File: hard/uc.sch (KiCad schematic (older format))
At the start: 1 part

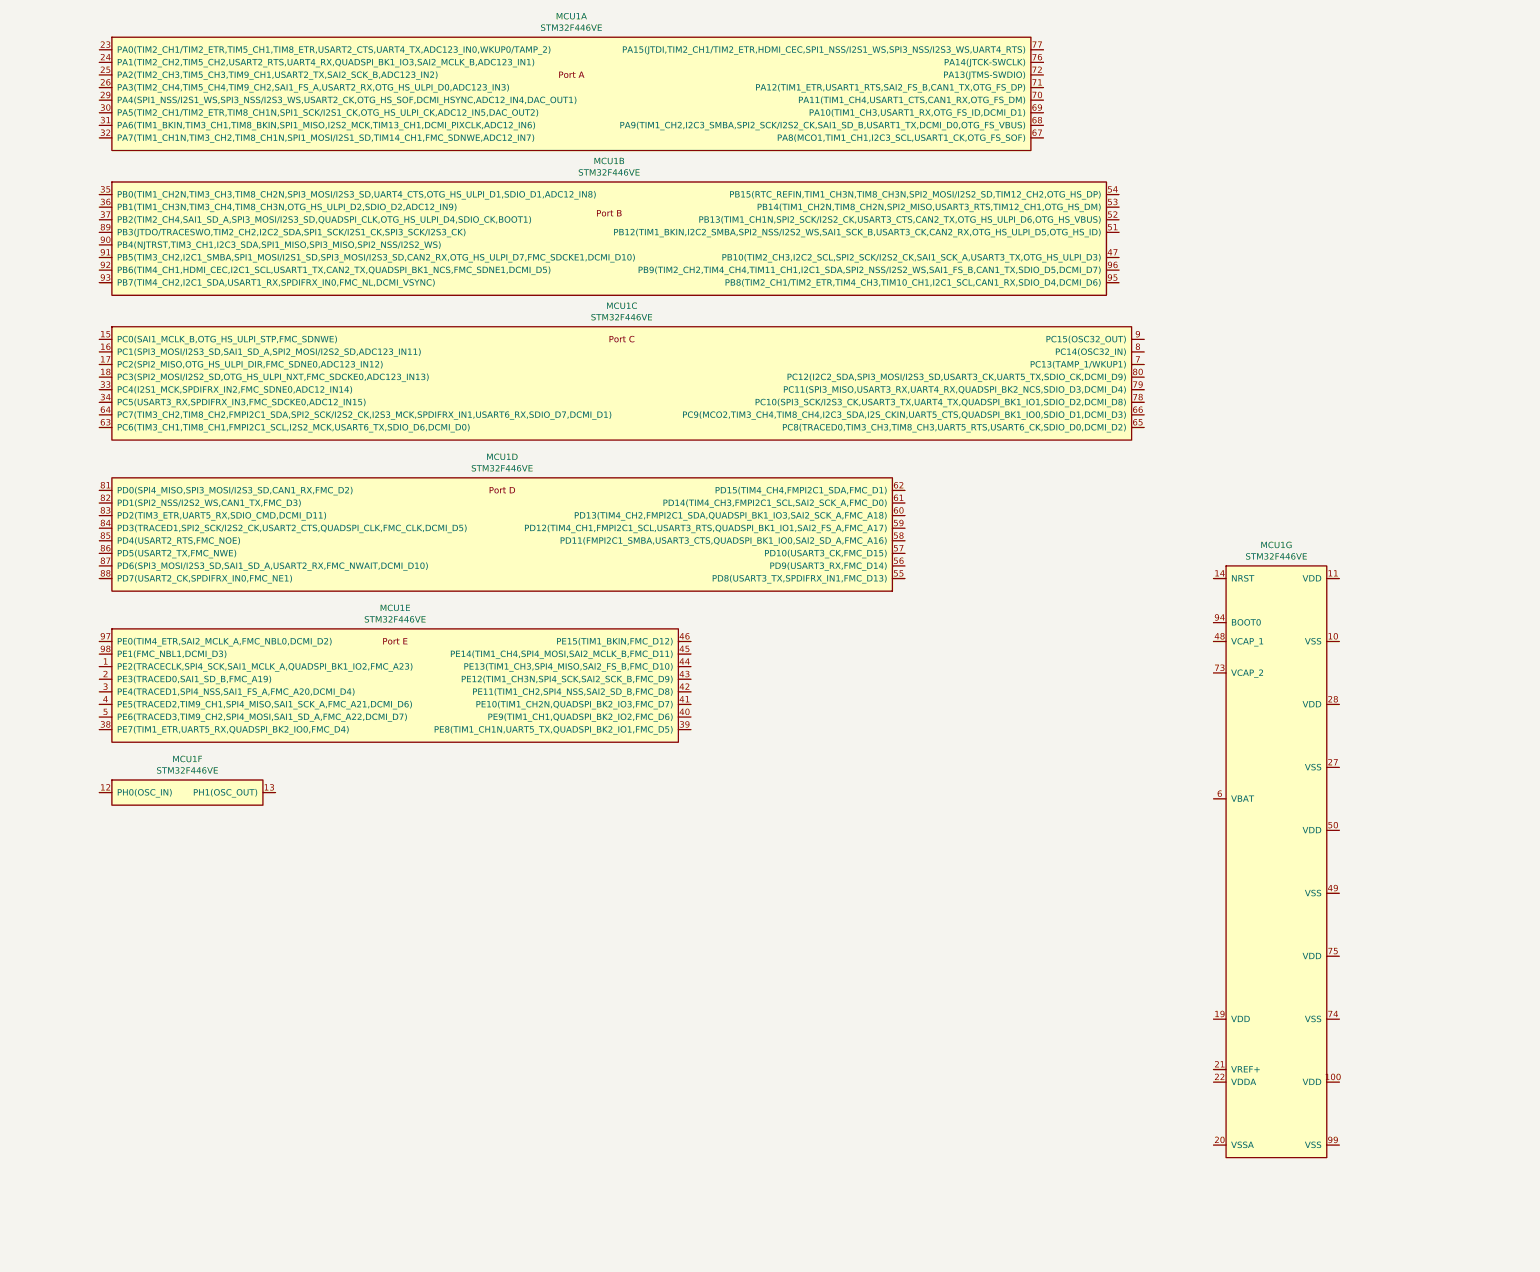
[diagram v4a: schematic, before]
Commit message: mcu progress sync to pcb
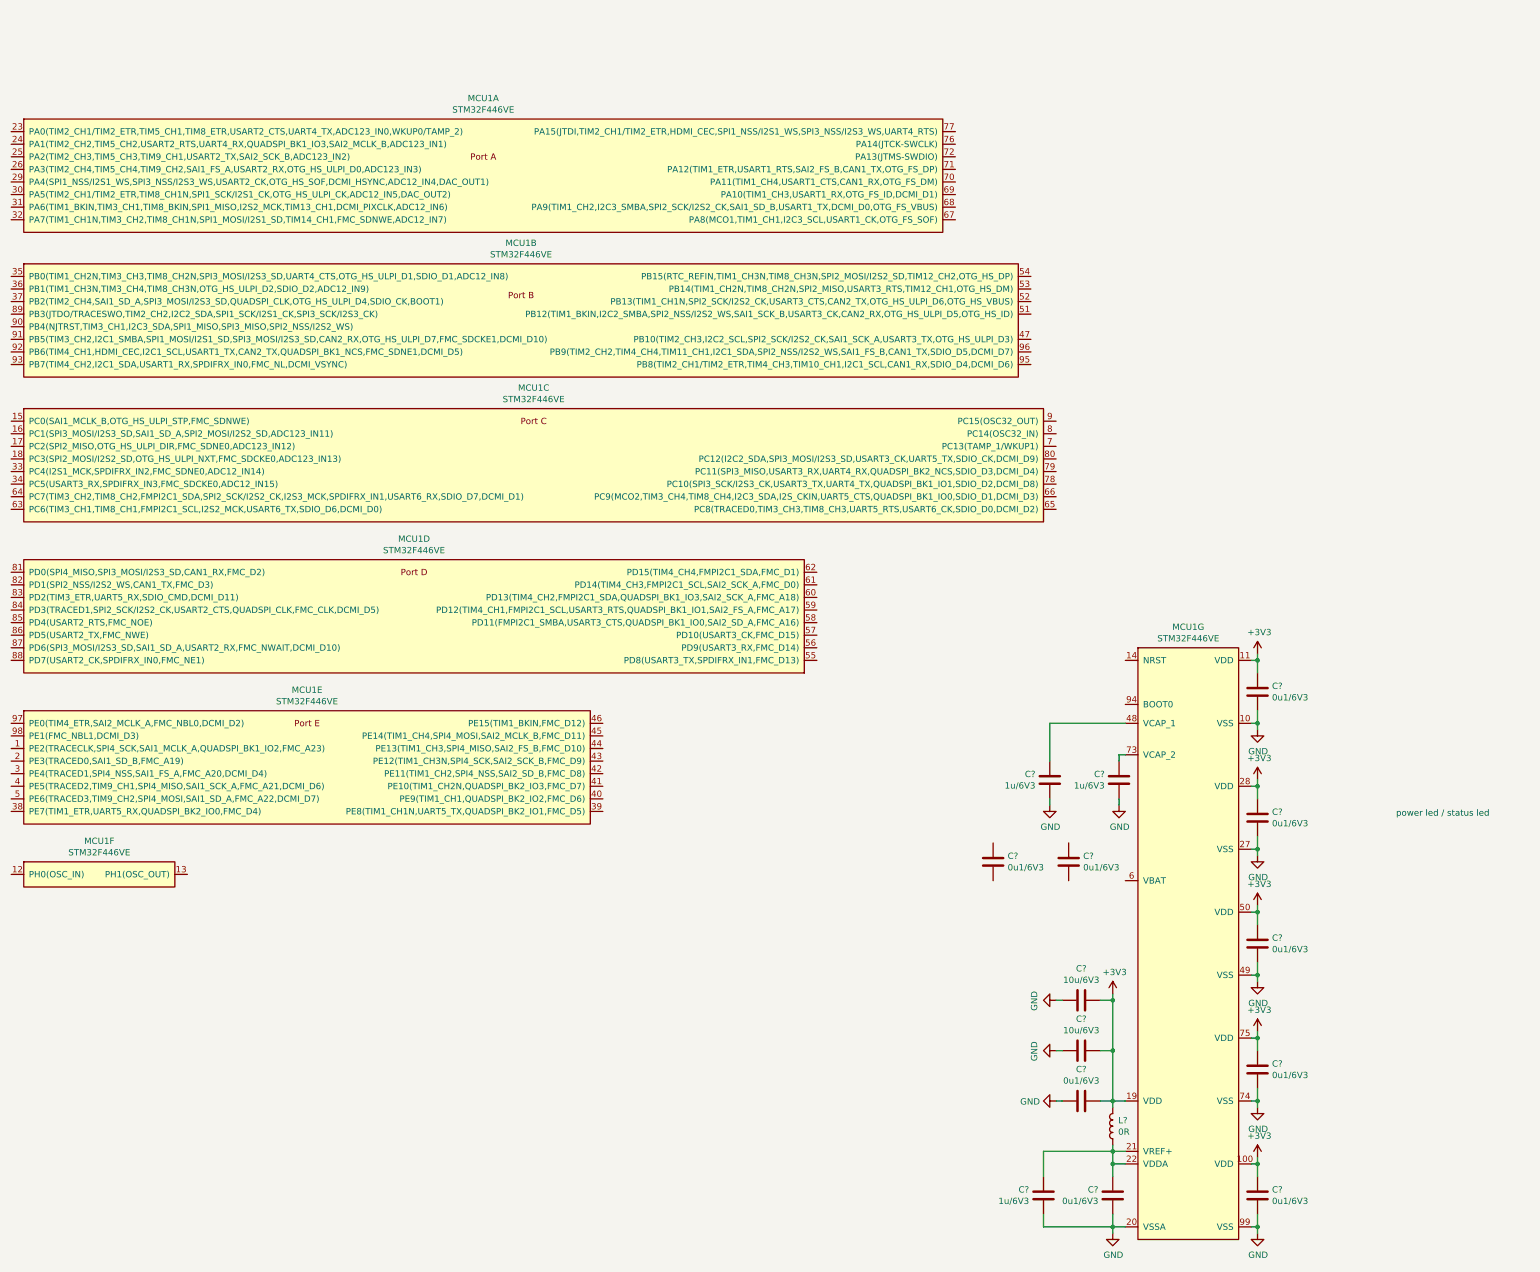
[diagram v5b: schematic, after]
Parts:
- added C? (x9): 0u1/6V3, Capacitor_SMD:C_0402_1005Metric, symbol Device:C
- added C? (x2): 10u/6V3, Capacitor_SMD:C_0805_2012Metric, symbol Device:C
- added C? (x3): 1u/6V3, Capacitor_SMD:C_0805_2012Metric, symbol Device:C
- added L?: 0R, Resistor_SMD:R_1206_3216Metric, symbol Device:L
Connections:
- net GND: now reaches MCU1.10 (VSS)
- net GND: now also MCU1.20 (VSSA), MCU1.27 (VSS), MCU1.49 (VSS), MCU1.74 (VSS), MCU1.99 (VSS), C?.1, C?.1, C?.1, C?.1, C?.1, C?.1, C?.1, C?.2, C?.2, C?.2, C?.2, C?.2
- net +3V3: now reaches MCU1.100 (VDD)
- net +3V3: now also MCU1.11 (VDD), MCU1.19 (VDD), MCU1.28 (VDD), MCU1.50 (VDD), MCU1.75 (VDD), C?.1, C?.1, C?.1, C?.1, C?.1, C?.2, C?.2, C?.2, L?.1
- net at MCU1.21 (VREF+): now also MCU1.22 (VDDA), C?.2, C?.2, L?.2
- net at MCU1.48 (VCAP_1): now also C?.2
- net at MCU1.73 (VCAP_2): now also C?.2
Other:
- note added: "power led / status led"
- moved on the sheet: MCU1A, MCU1B, MCU1C, MCU1D, MCU1E, MCU1F, MCU1G

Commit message: layouting update
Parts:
- gave numbers to parts that had none: 15
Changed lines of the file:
@@
 $EndComp
 $Comp
-L Device:C C?
+L Device:C C1
 U 1 1 61E65F1B
 P 13450 6450
-F 0 "C?" H 13565 6496 50  0000 L CNN
+F 0 "C1" H 13565 6496 50  0000 L CNN
 F 1 "0u1/6V3" H 13565 6405 50  0000 L CNN
 F 2 "Capacitor_SMD:C_0402_1005Metric" H 13488 6300 50  0001 C CNN
@@
 $EndComp
 $Comp
-L Device:C C?
+L Device:C C4
 U 1 1 61E6A345
 P 13450 7450
-F 0 "C?" H 13565 7496 50  0000 L CNN
+F 0 "C4" H 13565 7496 50  0000 L CNN
 F 1 "0u1/6V3" H 13565 7405 50  0000 L CNN
 F 2 "Capacitor_SMD:C_0402_1005Metric" H 13488 7300 50  0001 C CNN
@@
 $EndComp
 $Comp
-L Device:C C?
+L Device:C C7
 U 1 1 61E6AC65
 P 13450 8450
-F 0 "C?" H 13565 8496 50  0000 L CNN
+F 0 "C7" H 13565 8496 50  0000 L CNN
 F 1 "0u1/6V3" H 13565 8405 50  0000 L CNN
 F 2 "Capacitor_SMD:C_0402_1005Metric" H 13488 8300 50  0001 C CNN
@@
 $EndComp
 $Comp
-L Device:C C?
+L Device:C C10
 U 1 1 61E6B3AC
 P 13450 9450
-F 0 "C?" H 13565 9496 50  0000 L CNN
+F 0 "C10" H 13565 9496 50  0000 L CNN
 F 1 "0u1/6V3" H 13565 9405 50  0000 L CNN
 F 2 "Capacitor_SMD:C_0402_1005Metric" H 13488 9300 50  0001 C CNN
@@
 $EndComp
 $Comp
-L Device:C C?
+L Device:C C14
 U 1 1 61E6B995
 P 13450 10450
-F 0 "C?" H 13565 10496 50  0000 L CNN
+F 0 "C14" H 13565 10496 50  0000 L CNN
 F 1 "0u1/6V3" H 13565 10405 50  0000 L CNN
 F 2 "Capacitor_SMD:C_0402_1005Metric" H 13488 10300 50  0001 C CNN
@@
 $EndComp
 $Comp
-L Device:C C?
+L Device:C C9
 U 1 1 61E6C2BD
 P 12050 9300
-F 0 "C?" V 12302 9300 50  0000 C CNN
+F 0 "C9" V 12302 9300 50  0000 C CNN
 F 1 "10u/6V3" V 12211 9300 50  0000 C CNN
 F 2 "Capacitor_SMD:C_0805_2012Metric" H 12088 9150 50  0001 C CNN
@@
 $EndComp
 $Comp
-L Device:C C?
+L Device:C C5
 U 1 1 61E6D721
 P 11350 7800
-F 0 "C?" H 11235 7846 50  0000 R CNN
+F 0 "C5" H 11235 7846 50  0000 R CNN
 F 1 "0u1/6V3" H 11235 7755 50  0000 R CNN
 F 2 "Capacitor_SMD:C_0402_1005Metric" H 11388 7650 50  0001 C CNN
@@
 $EndComp
 $Comp
-L power:GND #PWR?
+L power:GND #PWR012
 U 1 1 61E75313
 P 11850 9300
-F 0 "#PWR?" H 11850 9050 50  0001 C CNN
+F 0 "#PWR012" H 11850 9050 50  0001 C CNN
 F 1 "GND" H 11855 9127 50  0000 C CNN
 F 2 "" H 11850 9300 50  0001 C CNN
@@
 $EndComp
 $Comp
-L Device:C C?
+L Device:C C6
 U 1 1 61E772DF
 P 11950 7800
-F 0 "C?" H 11835 7846 50  0000 R CNN
+F 0 "C6" H 11835 7846 50  0000 R CNN
 F 1 "0u1/6V3" H 11835 7755 50  0000 R CNN
 F 2 "Capacitor_SMD:C_0402_1005Metric" H 11988 7650 50  0001 C CNN
@@
 $EndComp
 $Comp
-L Device:C C?
+L Device:C C12
 U 1 1 61E78992
 P 11750 10450
-F 0 "C?" H 11636 10404 50  0000 R CNN
+F 0 "C12" H 11636 10404 50  0000 R CNN
 F 1 "1u/6V3" H 11636 10495 50  0000 R CNN
 F 2 "Capacitor_SMD:C_0805_2012Metric" H 11788 10300 50  0001 C CNN
@@
 $EndComp
 $Comp
-L Device:C C?
+L Device:C C13
 U 1 1 61E790B0
 P 12300 10450
-F 0 "C?" H 12186 10404 50  0000 R CNN
+F 0 "C13" H 12186 10404 50  0000 R CNN
 F 1 "0u1/6V3" H 12186 10495 50  0000 R CNN
 F 2 "Capacitor_SMD:C_0402_1005Metric" H 12338 10300 50  0001 C CNN
@@
 $EndComp
 $Comp
-L Device:L L?
+L Device:L L1
 U 1 1 61E7B501
 P 12300 9900
-F 0 "L?" H 12257 9946 50  0000 R CNN
+F 0 "L1" H 12257 9946 50  0000 R CNN
 F 1 "0R" H 12257 9855 50  0000 R CNN
 F 2 "Resistor_SMD:R_1206_3216Metric" H 12300 9900 50  0001 C CNN
@@
 power led / status led
 $Comp
-L power:+3V3 #PWR?
+L power:+3V3 #PWR09
 U 1 1 61E81AB1
 P 12300 8850
-F 0 "#PWR?" H 12300 8700 50  0001 C CNN
+F 0 "#PWR09" H 12300 8700 50  0001 C CNN
 F 1 "+3V3" H 12315 9023 50  0000 C CNN
 F 2 "" H 12300 8850 50  0001 C CNN
@@
 Connection ~ 12300 10700
 $Comp
-L power:GND #PWR?
+L power:GND #PWR016
 U 1 1 61E8A945
 P 12300 10750
-F 0 "#PWR?" H 12300 10500 50  0001 C CNN
+F 0 "#PWR016" H 12300 10500 50  0001 C CNN
 F 1 "GND" H 12305 10577 50  0000 C CNN
 F 2 "" H 12300 10750 50  0001 C CNN
@@
 	13450 6200 13400 6200
 $Comp
-L power:GND #PWR?
+L power:GND #PWR02
 U 1 1 61EA5867
 P 13450 6750
-F 0 "#PWR?" H 13450 6500 50  0001 C CNN
+F 0 "#PWR02" H 13450 6500 50  0001 C CNN
 F 1 "GND" H 13455 6577 50  0000 C CNN
 F 2 "" H 13450 6750 50  0001 C CNN
@@
 $EndComp
 $Comp
-L power:GND #PWR?
+L power:GND #PWR06
 U 1 1 61EA5DA3
 P 13450 7750
-F 0 "#PWR?" H 13450 7500 50  0001 C CNN
+F 0 "#PWR06" H 13450 7500 50  0001 C CNN
 F 1 "GND" H 13455 7577 50  0000 C CNN
 F 2 "" H 13450 7750 50  0001 C CNN
@@
 $EndComp
 $Comp
-L power:GND #PWR?
+L power:GND #PWR08
 U 1 1 61EA6251
 P 13450 8750
-F 0 "#PWR?" H 13450 8500 50  0001 C CNN
+F 0 "#PWR08" H 13450 8500 50  0001 C CNN
 F 1 "GND" H 13455 8577 50  0000 C CNN
 F 2 "" H 13450 8750 50  0001 C CNN
@@
 $EndComp
 $Comp
-L power:GND #PWR?
+L power:GND #PWR014
 U 1 1 61EA6951
 P 13450 9750
-F 0 "#PWR?" H 13450 9500 50  0001 C CNN
+F 0 "#PWR014" H 13450 9500 50  0001 C CNN
 F 1 "GND" H 13455 9577 50  0000 C CNN
 F 2 "" H 13450 9750 50  0001 C CNN
@@
 $EndComp
 $Comp
-L power:GND #PWR?
+L power:GND #PWR017
 U 1 1 61EA6F6D
 P 13450 10750
-F 0 "#PWR?" H 13450 10500 50  0001 C CNN
+F 0 "#PWR017" H 13450 10500 50  0001 C CNN
 F 1 "GND" H 13455 10577 50  0000 C CNN
 F 2 "" H 13450 10750 50  0001 C CNN
@@
 $EndComp
 $Comp
-L power:+3V3 #PWR?
+L power:+3V3 #PWR01
 U 1 1 61EA754B
 P 13450 6150
-F 0 "#PWR?" H 13450 6000 50  0001 C CNN
+F 0 "#PWR01" H 13450 6000 50  0001 C CNN
 F 1 "+3V3" H 13465 6323 50  0000 C CNN
 F 2 "" H 13450 6150 50  0001 C CNN
@@
 $EndComp
 $Comp
-L power:+3V3 #PWR?
+L power:+3V3 #PWR03
 U 1 1 61EA7B7A
 P 13450 7150
-F 0 "#PWR?" H 13450 7000 50  0001 C CNN
+F 0 "#PWR03" H 13450 7000 50  0001 C CNN
 F 1 "+3V3" H 13465 7323 50  0000 C CNN
 F 2 "" H 13450 7150 50  0001 C CNN
@@
 $EndComp
 $Comp
-L power:+3V3 #PWR?
+L power:+3V3 #PWR07
 U 1 1 61EA822F
 P 13450 8150
-F 0 "#PWR?" H 13450 8000 50  0001 C CNN
+F 0 "#PWR07" H 13450 8000 50  0001 C CNN
 F 1 "+3V3" H 13465 8323 50  0000 C CNN
 F 2 "" H 13450 8150 50  0001 C CNN
@@
 $EndComp
 $Comp
-L power:+3V3 #PWR?
+L power:+3V3 #PWR011
 U 1 1 61EA8D8A
 P 13450 9150
-F 0 "#PWR?" H 13450 9000 50  0001 C CNN
+F 0 "#PWR011" H 13450 9000 50  0001 C CNN
 F 1 "+3V3" H 13465 9323 50  0000 C CNN
 F 2 "" H 13450 9150 50  0001 C CNN
@@
 $EndComp
 $Comp
-L power:+3V3 #PWR?
+L power:+3V3 #PWR015
 U 1 1 61EA9784
 P 13450 10150
-F 0 "#PWR?" H 13450 10000 50  0001 C CNN
+F 0 "#PWR015" H 13450 10000 50  0001 C CNN
 F 1 "+3V3" H 13465 10323 50  0000 C CNN
 F 2 "" H 13450 10150 50  0001 C CNN
@@
 	12400 10200 12300 10200
 $Comp
-L Device:C C?
+L Device:C C11
 U 1 1 61EB9E18
 P 12050 9700
-F 0 "C?" V 12302 9700 50  0000 C CNN
+F 0 "C11" V 12302 9700 50  0000 C CNN
 F 1 "0u1/6V3" V 12211 9700 50  0000 C CNN
 F 2 "Capacitor_SMD:C_0402_1005Metric" H 12088 9550 50  0001 C CNN
@@
 	11900 9700 11850 9700
 $Comp
-L power:GND #PWR?
+L power:GND #PWR013
 U 1 1 61EBD6ED
 P 11850 9700
-F 0 "#PWR?" H 11850 9450 50  0001 C CNN
+F 0 "#PWR013" H 11850 9450 50  0001 C CNN
 F 1 "GND" V 11855 9572 50  0000 R CNN
 F 2 "" H 11850 9700 50  0001 C CNN
@@
 	11900 9300 11850 9300
 $Comp
-L Device:C C?
+L Device:C C8
 U 1 1 61EEC98D
 P 12050 8900
-F 0 "C?" V 12302 8900 50  0000 C CNN
+F 0 "C8" V 12302 8900 50  0000 C CNN
 F 1 "10u/6V3" V 12211 8900 50  0000 C CNN
 F 2 "Capacitor_SMD:C_0805_2012Metric" H 12088 8750 50  0001 C CNN
@@
 Connection ~ 12300 8900
 $Comp
-L power:GND #PWR?
+L power:GND #PWR010
 U 1 1 61EF00F8
 P 11850 8900
-F 0 "#PWR?" H 11850 8650 50  0001 C CNN
+F 0 "#PWR010" H 11850 8650 50  0001 C CNN
 F 1 "GND" H 11855 8727 50  0000 C CNN
 F 2 "" H 11850 8900 50  0001 C CNN
@@
 	11800 6700 11800 7000
 $Comp
-L Device:C C?
+L Device:C C2
 U 1 1 61EF79CF
 P 11800 7150
-F 0 "C?" H 11686 7104 50  0000 R CNN
+F 0 "C2" H 11686 7104 50  0000 R CNN
 F 1 "1u/6V3" H 11686 7195 50  0000 R CNN
 F 2 "Capacitor_SMD:C_0805_2012Metric" H 11838 7000 50  0001 C CNN
@@
 	12350 6950 12350 7000
 $Comp
-L Device:C C?
+L Device:C C3
 U 1 1 61EF6517
 P 12350 7150
-F 0 "C?" H 12236 7104 50  0000 R CNN
+F 0 "C3" H 12236 7104 50  0000 R CNN
 F 1 "1u/6V3" H 12236 7195 50  0000 R CNN
 F 2 "Capacitor_SMD:C_0805_2012Metric" H 12388 7000 50  0001 C CNN
@@
 $EndComp
 $Comp
-L power:GND #PWR?
+L power:GND #PWR05
 U 1 1 61F051A7
 P 12350 7350
-F 0 "#PWR?" H 12350 7100 50  0001 C CNN
+F 0 "#PWR05" H 12350 7100 50  0001 C CNN
 F 1 "GND" H 12355 7177 50  0000 C CNN
 F 2 "" H 12350 7350 50  0001 C CNN
@@
 $EndComp
 $Comp
-L power:GND #PWR?
+L power:GND #PWR04
 U 1 1 61F05684
 P 11800 7350
-F 0 "#PWR?" H 11800 7100 50  0001 C CNN
+F 0 "#PWR04" H 11800 7100 50  0001 C CNN
 F 1 "GND" H 11805 7177 50  0000 C CNN
 F 2 "" H 11800 7350 50  0001 C CNN
